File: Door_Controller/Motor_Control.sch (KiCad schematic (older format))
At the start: 15 parts

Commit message: WIP motor poles
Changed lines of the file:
@@
 $Descr A4 11693 8268
 encoding utf-8
-Sheet 5 7
+Sheet 5 8
 Title ""
 Date ""
@@
 Large Traces
 $Sheet
-S 7350 1900 500  800
+S 7250 1900 500  800
 U 60652F73
-F0 "Motor_Controller_Pole" 39
+F0 "Lock_DriveA" 39
 F1 "Motor_Controller_Pole.sch" 39
-F2 "Motor_Output" B R 7850 2250 39
-F3 "Motor_Input" B L 7350 2000 39
-F4 "Drive" I L 7350 2450 39
+F2 "Motor_Output" B R 7750 2250 39
+F3 "Motor_Input" B L 7250 2000 39
+F4 "Drive" I L 7250 2450 39
 $EndSheet
 $Sheet
@@
 F4 "Output_Power" B R 6850 2200 39
 $EndSheet
+$Sheet
+S 7250 2900 500  800
+U 60688E8B
+F0 "Lock_DriveB" 39
+F1 "Motor_Controller_Pole.sch" 39
+F2 "Motor_Output" B R 7750 3250 39
+F3 "Motor_Input" B L 7250 3000 39
+F4 "Drive" I L 7250 3450 39
+$EndSheet
+Wire Wire Line
+	6850 2200 6900 2200
+Wire Wire Line
+	7050 2200 7050 2000
+Wire Wire Line
+	7050 2000 7250 2000
+Wire Wire Line
+	6900 2200 6900 3000
+Wire Wire Line
+	6900 3000 7250 3000
+Connection ~ 6900 2200
+Wire Wire Line
+	6900 2200 7050 2200
 $EndSCHEMATC

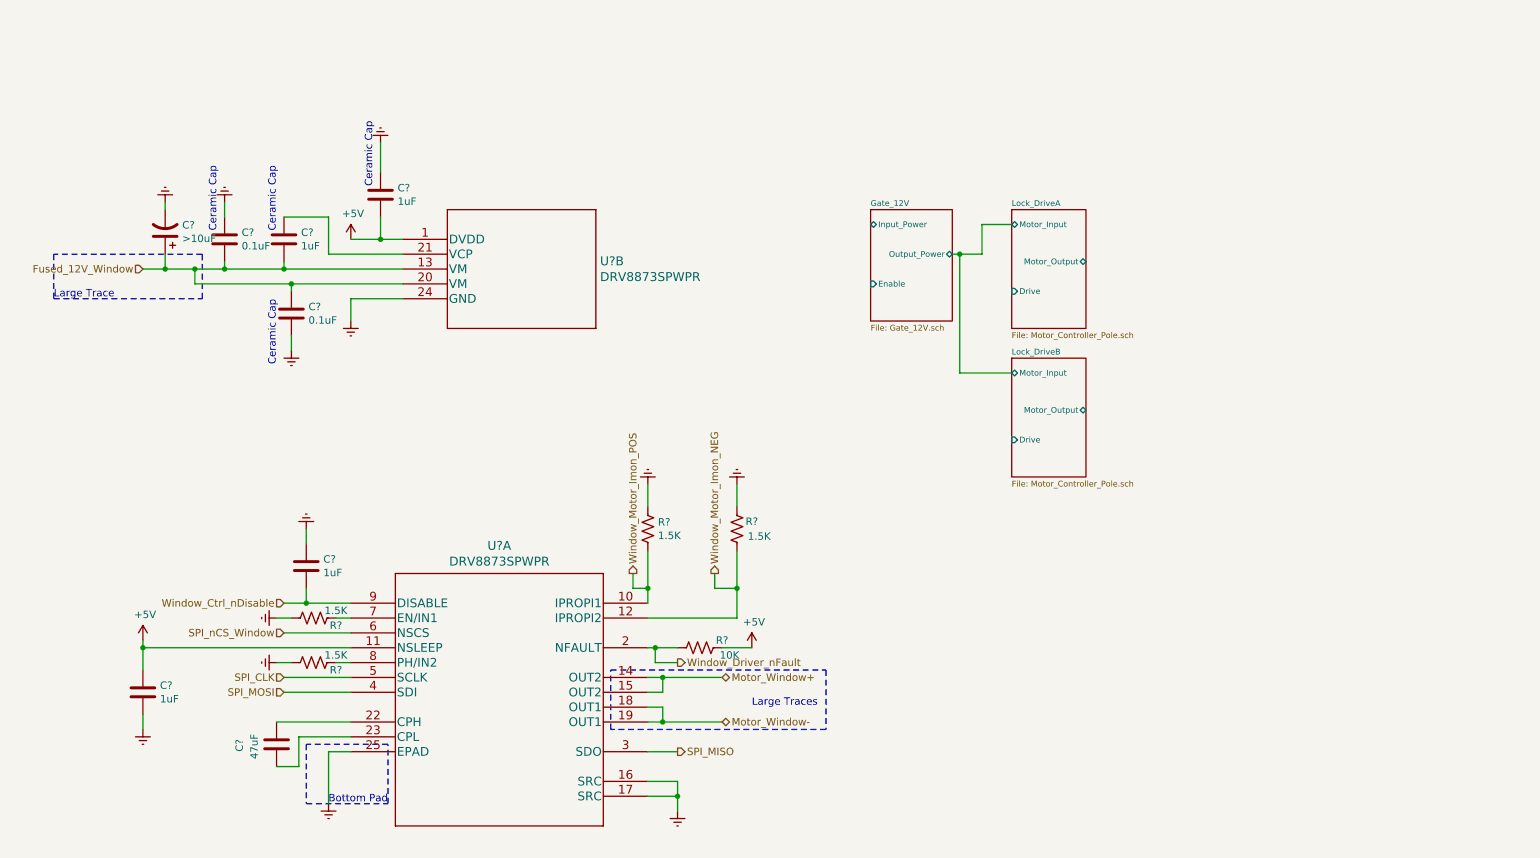
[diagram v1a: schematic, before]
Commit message: flesh out motor poles
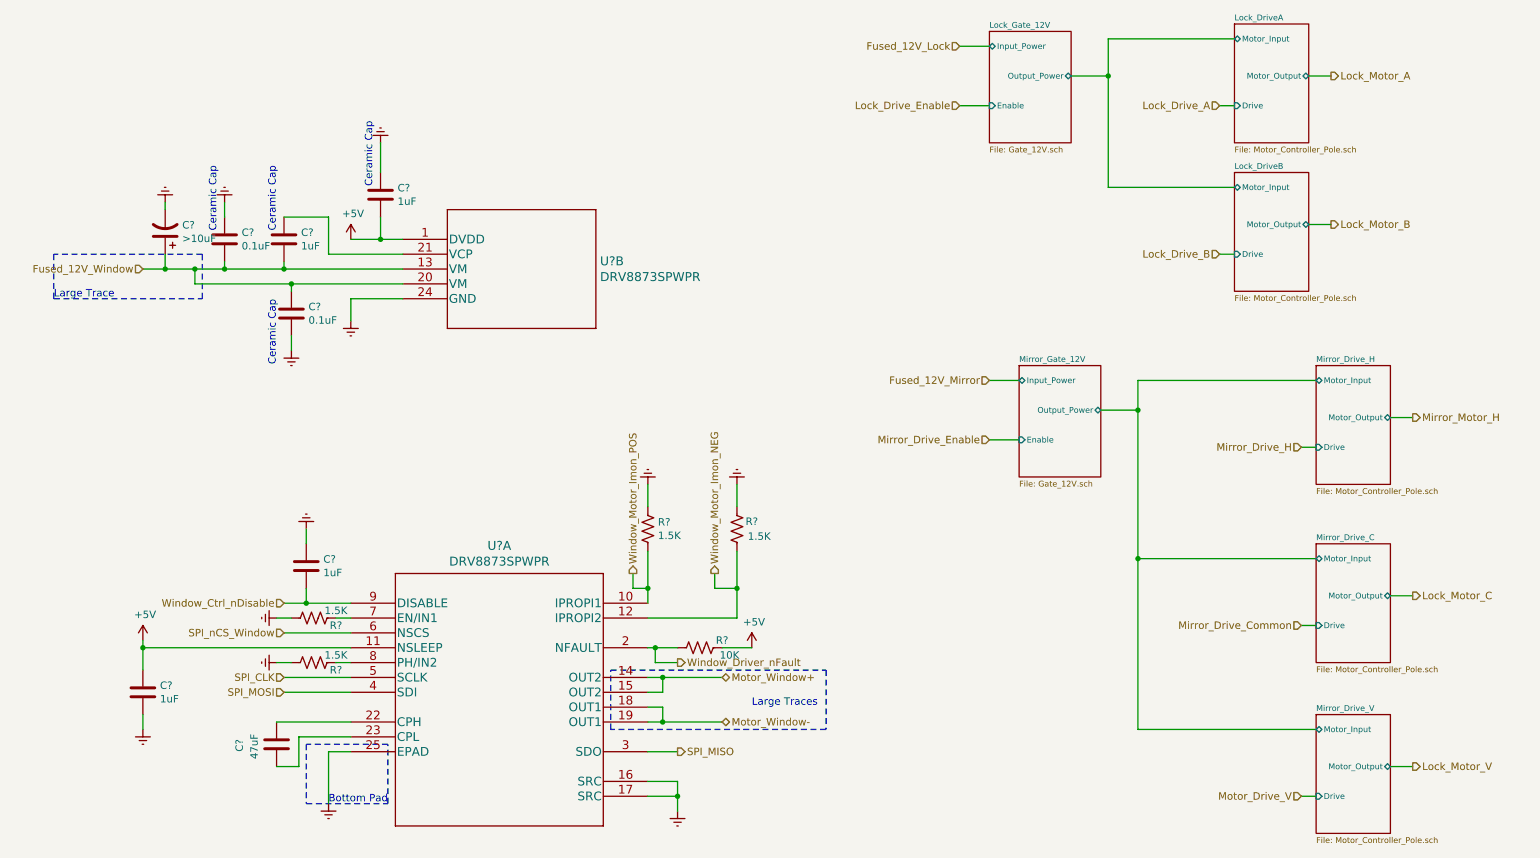
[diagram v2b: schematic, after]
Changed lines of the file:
@@
 Large Traces
 $Sheet
-S 7250 1900 500  800
+S 8750 650  500  800
 U 60652F73
 F0 "Lock_DriveA" 39
 F1 "Motor_Controller_Pole.sch" 39
-F2 "Motor_Output" B R 7750 2250 39
-F3 "Motor_Input" B L 7250 2000 39
-F4 "Drive" I L 7250 2450 39
+F2 "Motor_Output" B R 9250 1000 39
+F3 "Motor_Input" B L 8750 750 39
+F4 "Drive" I L 8750 1200 39
 $EndSheet
 $Sheet
-S 6300 1900 550  750
-U 60669CB5
-F0 "Gate_12V" 39
-F1 "Gate_12V.sch" 39
-F2 "Input_Power" B L 6300 2000 39
-F3 "Enable" I L 6300 2400 39
-F4 "Output_Power" B R 6850 2200 39
-$EndSheet
-$Sheet
-S 7250 2900 500  800
+S 8750 1650 500  800
 U 60688E8B
 F0 "Lock_DriveB" 39
 F1 "Motor_Controller_Pole.sch" 39
-F2 "Motor_Output" B R 7750 3250 39
-F3 "Motor_Input" B L 7250 3000 39
-F4 "Drive" I L 7250 3450 39
+F2 "Motor_Output" B R 9250 2000 39
+F3 "Motor_Input" B L 8750 1750 39
+F4 "Drive" I L 8750 2200 39
+$EndSheet
+Text HLabel 8650 2200 0    50   Input ~ 0
+Lock_Drive_B
+Text HLabel 9400 1000 2    50   Output ~ 0
+Lock_Motor_A
+Text HLabel 9400 2000 2    50   Output ~ 0
+Lock_Motor_B
+Wire Wire Line
+	8650 1200 8750 1200
+Wire Wire Line
+	8650 2200 8750 2200
+Wire Wire Line
+	9250 2000 9400 2000
+Wire Wire Line
+	9250 1000 9400 1000
+Wire Wire Line
+	6900 1200 7100 1200
+Text HLabel 8650 1200 0    50   Input ~ 0
+Lock_Drive_A
+Text HLabel 6900 1200 0    50   Input ~ 0
+Lock_Drive_Enable
+$Sheet
+S 7100 700  550  750
+U 60669CB5
+F0 "Lock_Gate_12V" 39
+F1 "Gate_12V.sch" 39
+F2 "Input_Power" B L 7100 800 39
+F3 "Enable" I L 7100 1200 39
+F4 "Output_Power" B R 7650 1000 39
 $EndSheet
 Wire Wire Line
-	6850 2200 6900 2200
+	6900 800  7100 800
+Text HLabel 6900 800  0    50   Input ~ 0
+Fused_12V_Lock
 Wire Wire Line
-	7050 2200 7050 2000
+	7100 3450 7300 3450
+Text HLabel 7100 3450 0    50   Input ~ 0
+Mirror_Drive_Enable
+$Sheet
+S 7300 2950 550  750
+U 60BA7C5A
+F0 "Mirror_Gate_12V" 39
+F1 "Gate_12V.sch" 39
+F2 "Input_Power" B L 7300 3050 39
+F3 "Enable" I L 7300 3450 39
+F4 "Output_Power" B R 7850 3250 39
+$EndSheet
 Wire Wire Line
-	7050 2000 7250 2000
+	7100 3050 7300 3050
+Text HLabel 7100 3050 0    50   Input ~ 0
+Fused_12V_Mirror
+$Sheet
+S 9300 2950 500  800
+U 60BAB905
+F0 "Mirror_Drive_H" 39
+F1 "Motor_Controller_Pole.sch" 39
+F2 "Motor_Output" B R 9800 3300 39
+F3 "Motor_Input" B L 9300 3050 39
+F4 "Drive" I L 9300 3500 39
+$EndSheet
+Text HLabel 9950 3300 2    50   Output ~ 0
+Mirror_Motor_H
 Wire Wire Line
-	6900 2200 6900 3000
+	9200 3500 9300 3500
 Wire Wire Line
-	6900 3000 7250 3000
-Connection ~ 6900 2200
+	9800 3300 9950 3300
+Text HLabel 9200 3500 0    50   Input ~ 0
+Mirror_Drive_H
 Wire Wire Line
-	6900 2200 7050 2200
+	7900 1000 7900 750
+Wire Wire Line
+	7900 750  8750 750
+Wire Wire Line
+	7650 1000 7900 1000
+Wire Wire Line
+	8750 1750 7900 1750
+Wire Wire Line
+	7900 1750 7900 1000
+Connection ~ 7900 1000
+$Sheet
+S 9300 4150 500  800
+U 60BC94D7
+F0 "Mirror_Drive_C" 39
+F1 "Motor_Controller_Pole.sch" 39
+F2 "Motor_Output" B R 9800 4500 39
+F3 "Motor_Input" B L 9300 4250 39
+F4 "Drive" I L 9300 4700 39
+$EndSheet
+Text HLabel 9950 4500 2    50   Output ~ 0
+Lock_Motor_C
+Wire Wire Line
+	9200 4700 9300 4700
+Wire Wire Line
+	9800 4500 9950 4500
+Text HLabel 9200 4700 0    50   Input ~ 0
+Mirror_Drive_Common
+$Sheet
+S 9300 5300 500  800
+U 60BCBDD0
+F0 "Mirror_Drive_V" 39
+F1 "Motor_Controller_Pole.sch" 39
+F2 "Motor_Output" B R 9800 5650 39
+F3 "Motor_Input" B L 9300 5400 39
+F4 "Drive" I L 9300 5850 39
+$EndSheet
+Text HLabel 9950 5650 2    50   Output ~ 0
+Lock_Motor_V
+Wire Wire Line
+	9200 5850 9300 5850
+Wire Wire Line
+	9800 5650 9950 5650
+Text HLabel 9200 5850 0    50   Input ~ 0
+Motor_Drive_V
+Wire Wire Line
+	7850 3250 8100 3250
+Wire Wire Line
+	8100 3250 8100 3050
+Wire Wire Line
+	8100 3050 9300 3050
+Wire Wire Line
+	9300 4250 8100 4250
+Wire Wire Line
+	8100 4250 8100 3250
+Connection ~ 8100 3250
+Wire Wire Line
+	9300 5400 8100 5400
+Wire Wire Line
+	8100 5400 8100 4250
+Connection ~ 8100 4250
 $EndSCHEMATC

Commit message: update motor control pins
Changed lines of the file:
@@
 $Descr A4 11693 8268
 encoding utf-8
-Sheet 5 8
+Sheet 5 12
 Title ""
 Date ""
@@
 $EndSheet
 Text HLabel 9950 4500 2    50   Output ~ 0
-Lock_Motor_C
+Mirror_Motor_C
 Wire Wire Line
 	9200 4700 9300 4700
@@
 $EndSheet
 Text HLabel 9950 5650 2    50   Output ~ 0
-Lock_Motor_V
+Mirror_Motor_V
 Wire Wire Line
 	9200 5850 9300 5850
